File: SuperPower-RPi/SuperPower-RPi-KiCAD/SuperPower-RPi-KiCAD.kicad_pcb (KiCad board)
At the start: 2 copper layers, 65 x 56.5 mm, 119 parts, among them J1 Raspberry_Pi_2_3, J10 Conn_01x04, J11 QWIIC_Connector, J12 DNP, J13 Conn_01x06, J2 JST-PH, J3 DNP, J4 DNP, J5 DNP, J6 USB_C_Receptacle_USB2.0, J7 Conn_01x03, J8 Conn_02x05_Odd_Even, J9 Conn_01x02, Q1 Q_PMOS_DMP3056L-7_SOT-23, Q2 Q_PMOS_DMP3056L-7_SOT-23, Q3 Q_PMOS_DMP3056L-7_SOT-23, Q6 2N7002-7-F, Q7 Q_PMOS_DMP3056L-7_SOT-23, SW1 Tact, U1 TPS61088, U2 BQ25895RTW, U3 STM32F412RETx, U4 ATtiny85-20SU, U5 ME6210A33M3G, U6 NCP380HMU21AATBG

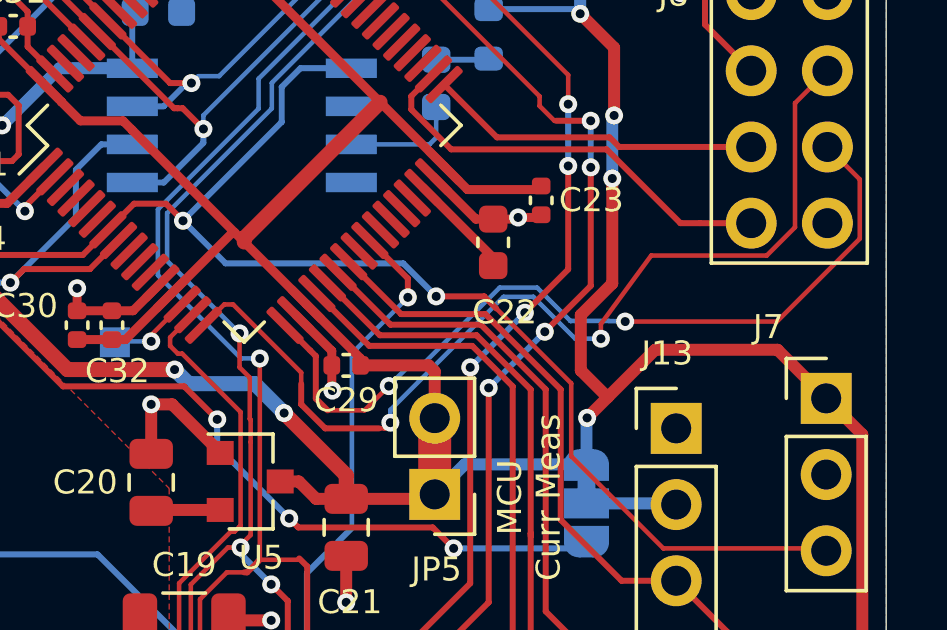
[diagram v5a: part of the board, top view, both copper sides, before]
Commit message: Optimized some traces.
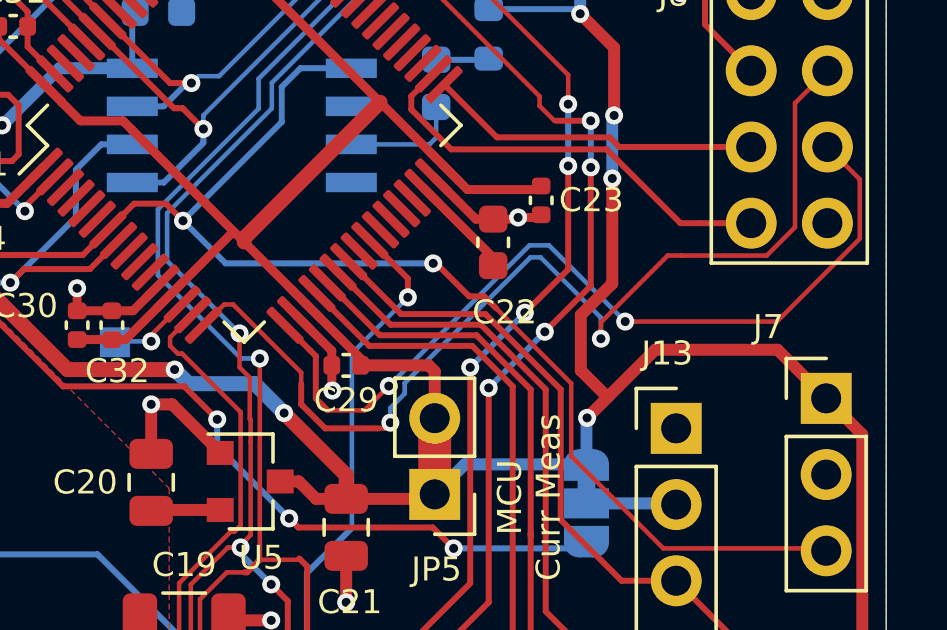
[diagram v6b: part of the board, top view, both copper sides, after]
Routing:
- net /Pi-MCU/UART_TX: track 32.7 -> 34.2 mm
- net /Pi-MCU/UART_RX: track 28.0 -> 29.1 mm
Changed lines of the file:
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@@
     (thickness 1.6)
     (drawings 55)
-    (tracks 1190)
+    (tracks 1191)
     (zones 0)
     (modules 119)
@@
   (page A4)
   (layers
-    (0 F.Cu signal hide)
+    (0 F.Cu signal)
     (31 B.Cu signal)
     (34 B.Paste user)
@@
   )
   (setup
-    (last_trace_width 0.2)
+    (last_trace_width 0.153)
     (user_trace_width 0.2)
     (user_trace_width 0.3)
@@
   (segment (start 74.35 60.05) (end 74.35 58.87) (width 0.2) (layer F.Cu) (net 12))
   (segment (start 74.2 60.2) (end 74.35 60.05) (width 0.2) (layer F.Cu) (net 12))
-  (via (at 100 72.6) (size 0.6) (drill 0.3) (layers F.Cu B.Cu) (net 12))
-  (segment (start 100 72.6) (end 101.6 72.6) (width 0.2) (layer F.Cu) (net 12))
   (segment (start 101.6 72.6) (end 102 73) (width 0.2) (layer F.Cu) (net 12))
   (segment (start 112.920499 81.000499) (end 113 81.08) (width 0.153) (layer F.Cu) (net 12))
@@
   (segment (start 89.92934 69.51) (end 90.99 69.51) (width 0.2) (layer F.Cu) (net 12))
   (segment (start 90.99 69.51) (end 91.56 70.08) (width 0.2) (layer F.Cu) (net 12))
-  (segment (start 91.56 70.08) (end 92.98 71.5) (width 0.2) (layer B.Cu) (net 12))
   (segment (start 94.85 66.79) (end 94.85 65.62) (width 0.2) (layer B.Cu) (net 12))
   (segment (start 95.475 64.995) (end 97.17 64.995) (width 0.2) (layer B.Cu) (net 12))
   (segment (start 91.56 70.08) (end 94.85 66.79) (width 0.2) (layer B.Cu) (net 12))
   (segment (start 94.85 65.62) (end 95.475 64.995) (width 0.2) (layer B.Cu) (net 12))
-  (segment (start 98.9 71.5) (end 100 72.6) (width 0.2) (layer B.Cu) (net 12))
-  (segment (start 92.98 71.5) (end 98.9 71.5) (width 0.2) (layer B.Cu) (net 12))
   (segment (start 72.89 65.61) (end 72.95 65.55) (width 0.2) (layer F.Cu) (net 12))
   (segment (start 72.89 67.86) (end 72.89 65.61) (width 0.2) (layer F.Cu) (net 12))
@@
   (segment (start 75.91 65.55) (end 77.05 65.55) (width 0.2) (layer F.Cu) (net 12))
   (segment (start 72.95 65.55) (end 75.91 65.55) (width 0.2) (layer F.Cu) (net 12))
+  (segment (start 101.6 72.6) (end 101.1 72.6) (width 0.2) (layer F.Cu) (net 12))
+  (via (at 99.9 71.5) (size 0.6) (drill 0.3) (layers F.Cu B.Cu) (net 12))
+  (segment (start 100 71.5) (end 99.9 71.5) (width 0.2) (layer F.Cu) (net 12))
+  (segment (start 101.1 72.6) (end 100 71.5) (width 0.2) (layer F.Cu) (net 12))
+  (segment (start 92.98 71.5) (end 91.56 70.08) (width 0.2) (layer B.Cu) (net 12))
+  (segment (start 99.9 71.5) (end 92.98 71.5) (width 0.2) (layer B.Cu) (net 12))
   (segment (start 72.29 97.09) (end 72.4 97.2) (width 0.2) (layer F.Cu) (net 13))
   (segment (start 70.2 97.09) (end 72.29 97.09) (width 0.2) (layer F.Cu) (net 13))
@@
   (segment (start 98.42 75.59) (end 97.61 76.4) (width 0.153) (layer F.Cu) (net 112))
   (segment (start 97.61 76.4) (end 96.381558 76.4) (width 0.153) (layer F.Cu) (net 112))
-  (segment (start 98.42 75.59) (end 99.14 74.87) (width 0.153) (layer B.Cu) (net 112))
-  (segment (start 99.14 74.87) (end 99.554091 74.87) (width 0.153) (layer B.Cu) (net 112))
-  (segment (start 99.554091 74.87) (end 102.114601 72.309489) (width 0.153) (layer B.Cu) (net 112))
-  (segment (start 102.114601 72.309489) (end 103.365913 72.309489) (width 0.153) (layer B.Cu) (net 112))
-  (segment (start 103.365913 72.309489) (end 104.476424 73.42) (width 0.153) (layer B.Cu) (net 112))
   (segment (start 95.8 74.4033) (end 95.986999 74.590299) (width 0.2) (layer F.Cu) (net 112))
   (segment (start 95.986999 74.590299) (end 95.986999 76.005441) (width 0.2) (layer F.Cu) (net 112))
   (segment (start 95.986999 76.005441) (end 96.381558 76.4) (width 0.2) (layer F.Cu) (net 112))
-  (segment (start 104.476424 73.42) (end 104.48 73.42) (width 0.153) (layer B.Cu) (net 112))
   (segment (start 114.119501 68.699501) (end 113.04 67.62) (width 0.153) (layer F.Cu) (net 112))
   (via (at 106.3 73.44) (size 0.6) (drill 0.3) (layers F.Cu B.Cu) (net 112))
   (segment (start 106.3 73.44) (end 111.357662 73.44) (width 0.153) (layer F.Cu) (net 112))
-  (segment (start 106.3 73.44) (end 105.75 73.42) (width 0.153) (layer B.Cu) (net 112))
-  (segment (start 105.75 73.42) (end 104.476424 73.42) (width 0.153) (layer B.Cu) (net 112))
   (segment (start 114.119501 70.678161) (end 114.119501 68.699501) (width 0.153) (layer F.Cu) (net 112))
   (segment (start 111.357662 73.44) (end 114.119501 70.678161) (width 0.153) (layer F.Cu) (net 112))
+  (segment (start 104.16 71.3) (end 106.3 73.44) (width 0.153) (layer B.Cu) (net 112))
+  (segment (start 103.76 70.9) (end 104.16 71.3) (width 0.153) (layer B.Cu) (net 112))
+  (segment (start 103.11 70.9) (end 103.76 70.9) (width 0.153) (layer B.Cu) (net 112))
+  (segment (start 98.42 75.59) (end 103.11 70.9) (width 0.153) (layer B.Cu) (net 112))
   (segment (start 95.5 75.518442) (end 95.5 76.2) (width 0.2) (layer F.Cu) (net 113))
   (segment (start 95.5 76.2) (end 96.3 77) (width 0.2) (layer F.Cu) (net 113))
@@
   (segment (start 98.281117 77) (end 98.471351 76.809766) (width 0.153) (layer F.Cu) (net 113))
   (segment (start 98.1 77) (end 98.281117 77) (width 0.153) (layer F.Cu) (net 113))
-  (segment (start 102.241354 72.615499) (end 98.471351 76.385502) (width 0.153) (layer B.Cu) (net 113))
-  (segment (start 103.239161 72.615499) (end 102.241354 72.615499) (width 0.153) (layer B.Cu) (net 113))
-  (segment (start 98.471351 76.385502) (end 98.471351 76.809766) (width 0.153) (layer B.Cu) (net 113))
-  (segment (start 104.633662 74.01) (end 103.239161 72.615499) (width 0.153) (layer B.Cu) (net 113))
-  (segment (start 105.49 74.01) (end 104.633662 74.01) (width 0.153) (layer B.Cu) (net 113))
   (via (at 105.49 74.01) (size 0.6) (drill 0.3) (layers F.Cu B.Cu) (net 113))
   (segment (start 111.960499 66.159501) (end 113.04 65.08) (width 0.153) (layer F.Cu) (net 113))
   (segment (start 111.960499 70.297163) (end 111.960499 66.159501) (width 0.153) (layer F.Cu) (net 113))
   (segment (start 111.018161 71.239501) (end 111.960499 70.297163) (width 0.153) (layer F.Cu) (net 113))
-  (segment (start 107.166235 71.239501) (end 111.018161 71.239501) (width 0.153) (layer F.Cu) (net 113))
-  (segment (start 105.49 73.52) (end 107.166235 71.239501) (width 0.153) (layer F.Cu) (net 113))
-  (segment (start 105.49 74.01) (end 105.49 73.52) (width 0.153) (layer F.Cu) (net 113))
   (segment (start 92.238819 73.564481) (end 92.9333 72.87) (width 0.153) (layer F.Cu) (net 113))
   (segment (start 92.9333 72.87) (end 93.23 72.87) (width 0.153) (layer F.Cu) (net 113))
   (segment (start 95.5 75.14) (end 95.5 75.518442) (width 0.153) (layer F.Cu) (net 113))
   (segment (start 93.23 72.87) (end 95.5 75.14) (width 0.153) (layer F.Cu) (net 113))
+  (segment (start 107.716837 71.239501) (end 108.160499 71.239501) (width 0.153) (layer F.Cu) (net 113))
+  (segment (start 105.49 73.466338) (end 107.716837 71.239501) (width 0.153) (layer F.Cu) (net 113))
+  (segment (start 105.49 74.01) (end 105.49 73.466338) (width 0.153) (layer F.Cu) (net 113))
+  (segment (start 108.160499 71.239501) (end 111.018161 71.239501) (width 0.153) (layer F.Cu) (net 113))
+  (segment (start 98.471351 76.385502) (end 98.471351 76.809766) (width 0.153) (layer B.Cu) (net 113))
+  (segment (start 98.471351 76.322311) (end 98.471351 76.385502) (width 0.153) (layer B.Cu) (net 113))
+  (segment (start 98.949501 75.844161) (end 98.471351 76.322311) (width 0.153) (layer B.Cu) (net 113))
+  (segment (start 98.949501 75.493261) (end 98.949501 75.844161) (width 0.153) (layer B.Cu) (net 113))
+  (segment (start 103.142762 71.3) (end 98.949501 75.493261) (width 0.153) (layer B.Cu) (net 113))
+  (segment (start 103.48 71.3) (end 103.142762 71.3) (width 0.153) (layer B.Cu) (net 113))
+  (segment (start 105.49 73.31) (end 103.48 71.3) (width 0.153) (layer B.Cu) (net 113))
+  (segment (start 105.49 74.01) (end 105.49 73.31) (width 0.153) (layer B.Cu) (net 113))
   (via (at 78.6 91) (size 0.6) (drill 0.3) (layers F.Cu B.Cu) (net 114))
   (segment (start 77.625 91.975) (end 78.6 91) (width 0.2) (layer B.Cu) (net 114))

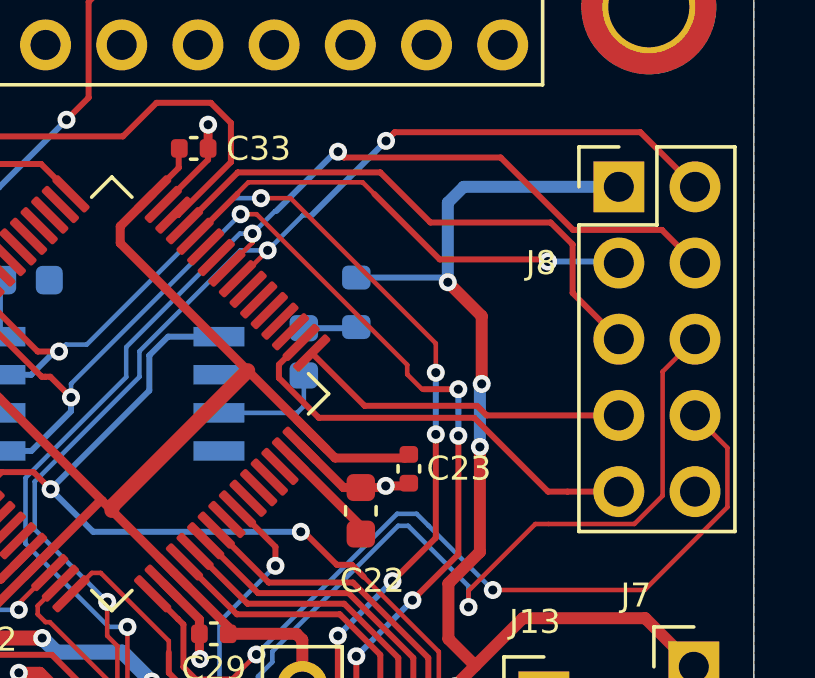
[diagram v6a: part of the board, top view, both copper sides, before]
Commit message: Connected LED0 to edge connector (J8.6) to accomodate an offboard button.
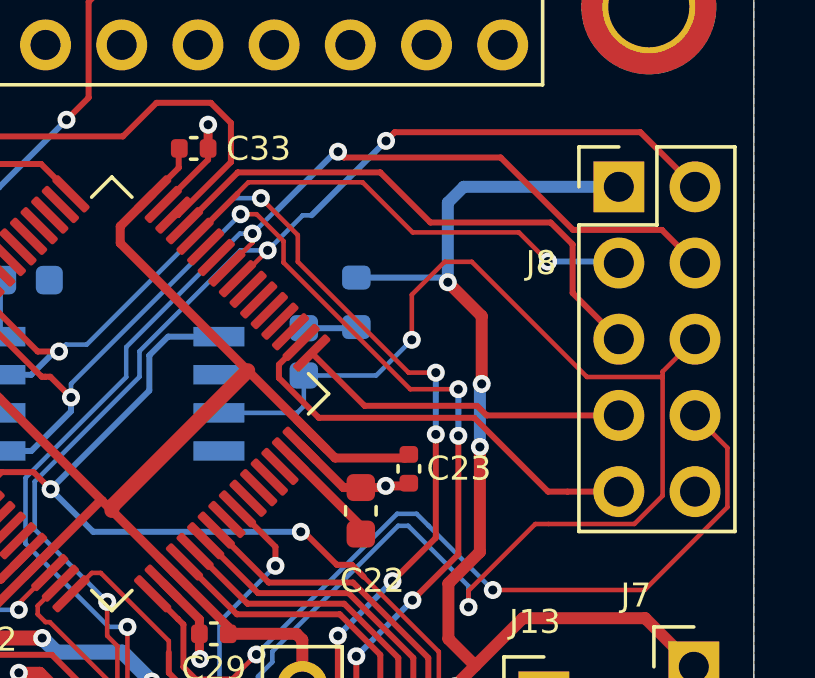
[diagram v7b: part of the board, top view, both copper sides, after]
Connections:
- D8 pad 1: /Pi-MCU/LED0 -> /Pi-MCU/UART_TX_LED0
- J8 pad 6: /Pi-MCU/UART_TX -> /Pi-MCU/UART_TX_LED0
- U3 pad 16: /Pi-MCU/UART_TX -> /Pi-MCU/UART_TX_LED0
- U4 pad 3: /Pi-MCU/LED0 -> /Pi-MCU/UART_TX_LED0
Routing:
- net /Pi-MCU/UART_TX_LED0: track 0.00 -> 54.2 mm, vias 0 -> 3
- net /Pi-MCU/UART_TX: track 34.2 -> 0.00 mm, vias 2 -> 0
- net /Pi-MCU/LED0: track 3.98 -> 0.00 mm

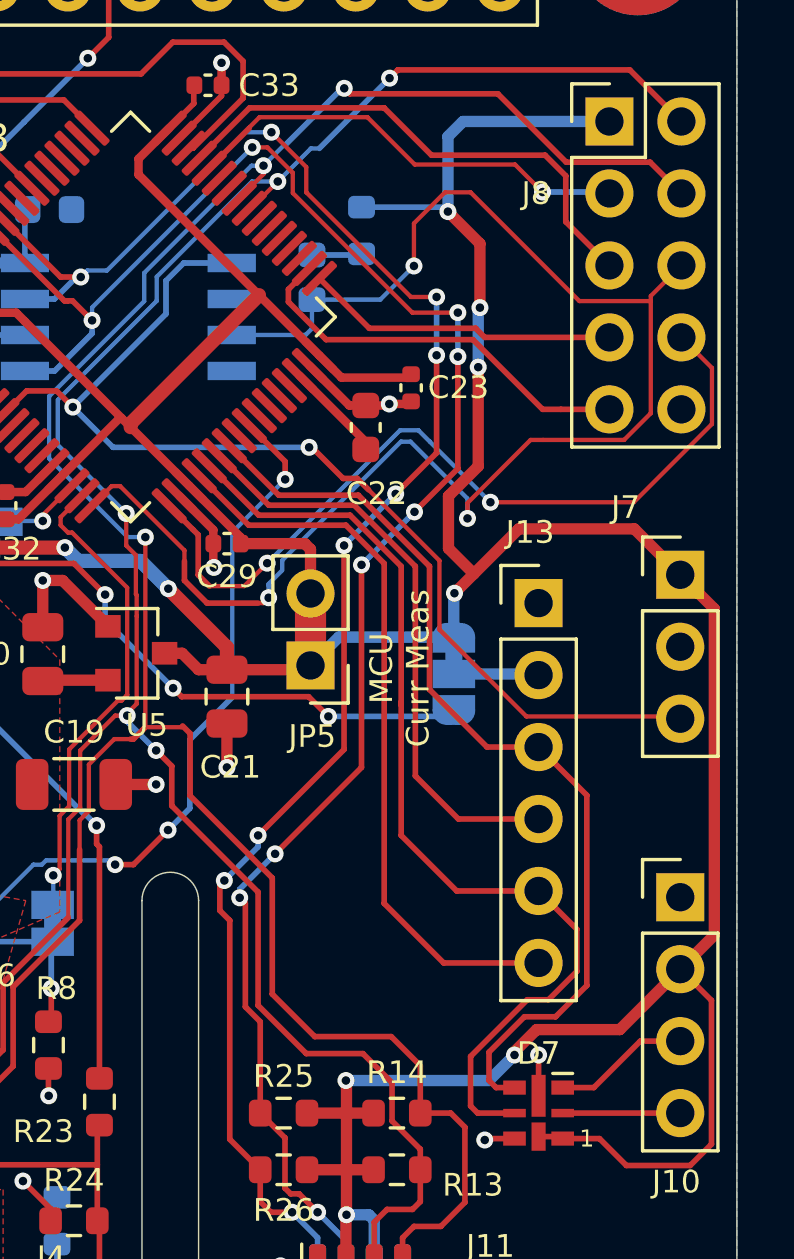
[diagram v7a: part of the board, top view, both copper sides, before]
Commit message: Added User button to schematic and PCB.
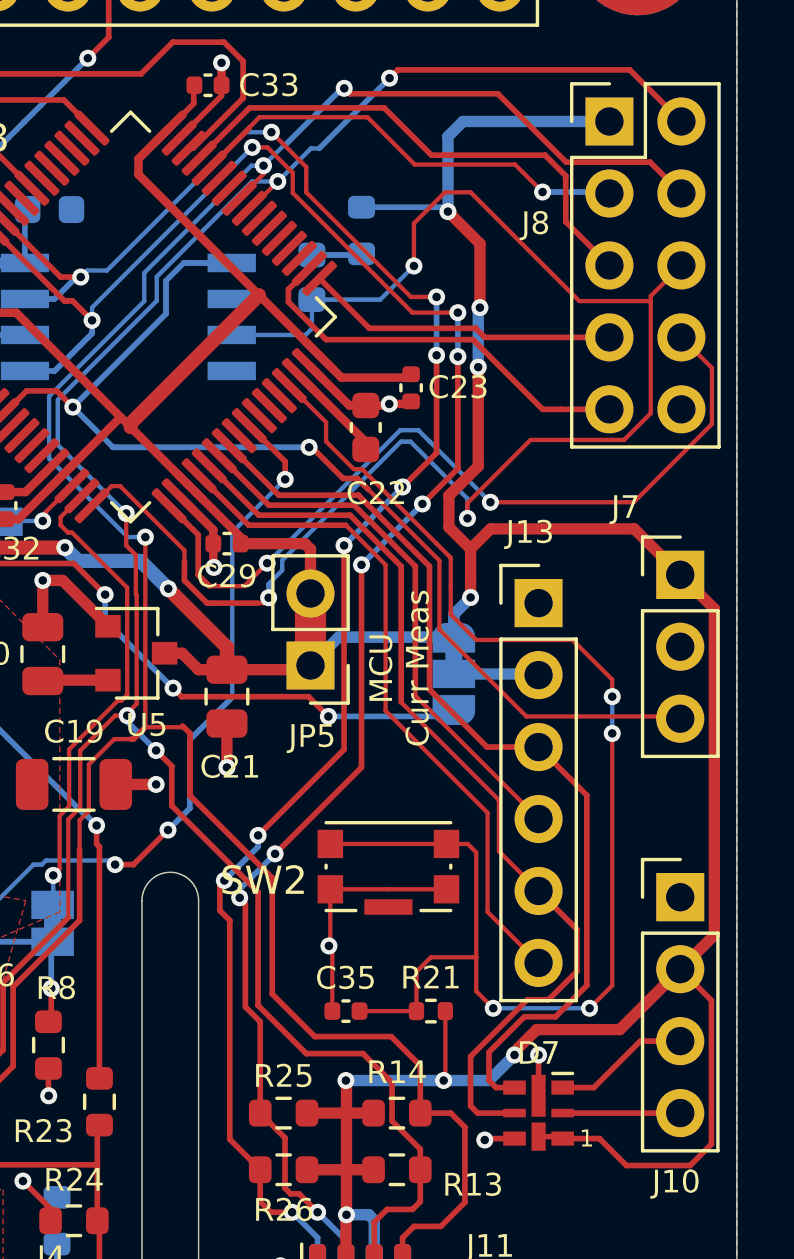
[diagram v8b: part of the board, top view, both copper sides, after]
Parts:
- added C35: 0.1uF, Capacitor_SMD:C_0402_1005Metric, F.Cu at (101.2, 91.4)
- added R21: 100k, Resistor_SMD:R_0402_1005Metric, F.Cu at (104.2, 91.4)
- added SW2: Tact, Button_Switch_SMD:SW_Push_1P1T-SH_NO_CK_KMR2xxG, F.Cu at (102.7, 86.3)
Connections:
- U3 pad 29: Net-(U3-Pad29) -> /Pi-MCU/USER_BUTTON
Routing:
- net /Pi-MCU/USER_BUTTON: track 0.00 -> 49.3 mm, vias 0 -> 4
- net GND: track 91.7 -> 100.1 mm, vias 42 -> 43
- net +3V3: track 143.8 -> 145.9 mm, vias 9 -> 10
- net /Pi-MCU/HW_NSS: track 26.1 -> 24.2 mm
- net /Pi-MCU/SCK: track 35.3 -> 33.5 mm
- net /Pi-MCU/MISO: track 20.9 -> 19.3 mm
